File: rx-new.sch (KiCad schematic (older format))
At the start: 56 parts

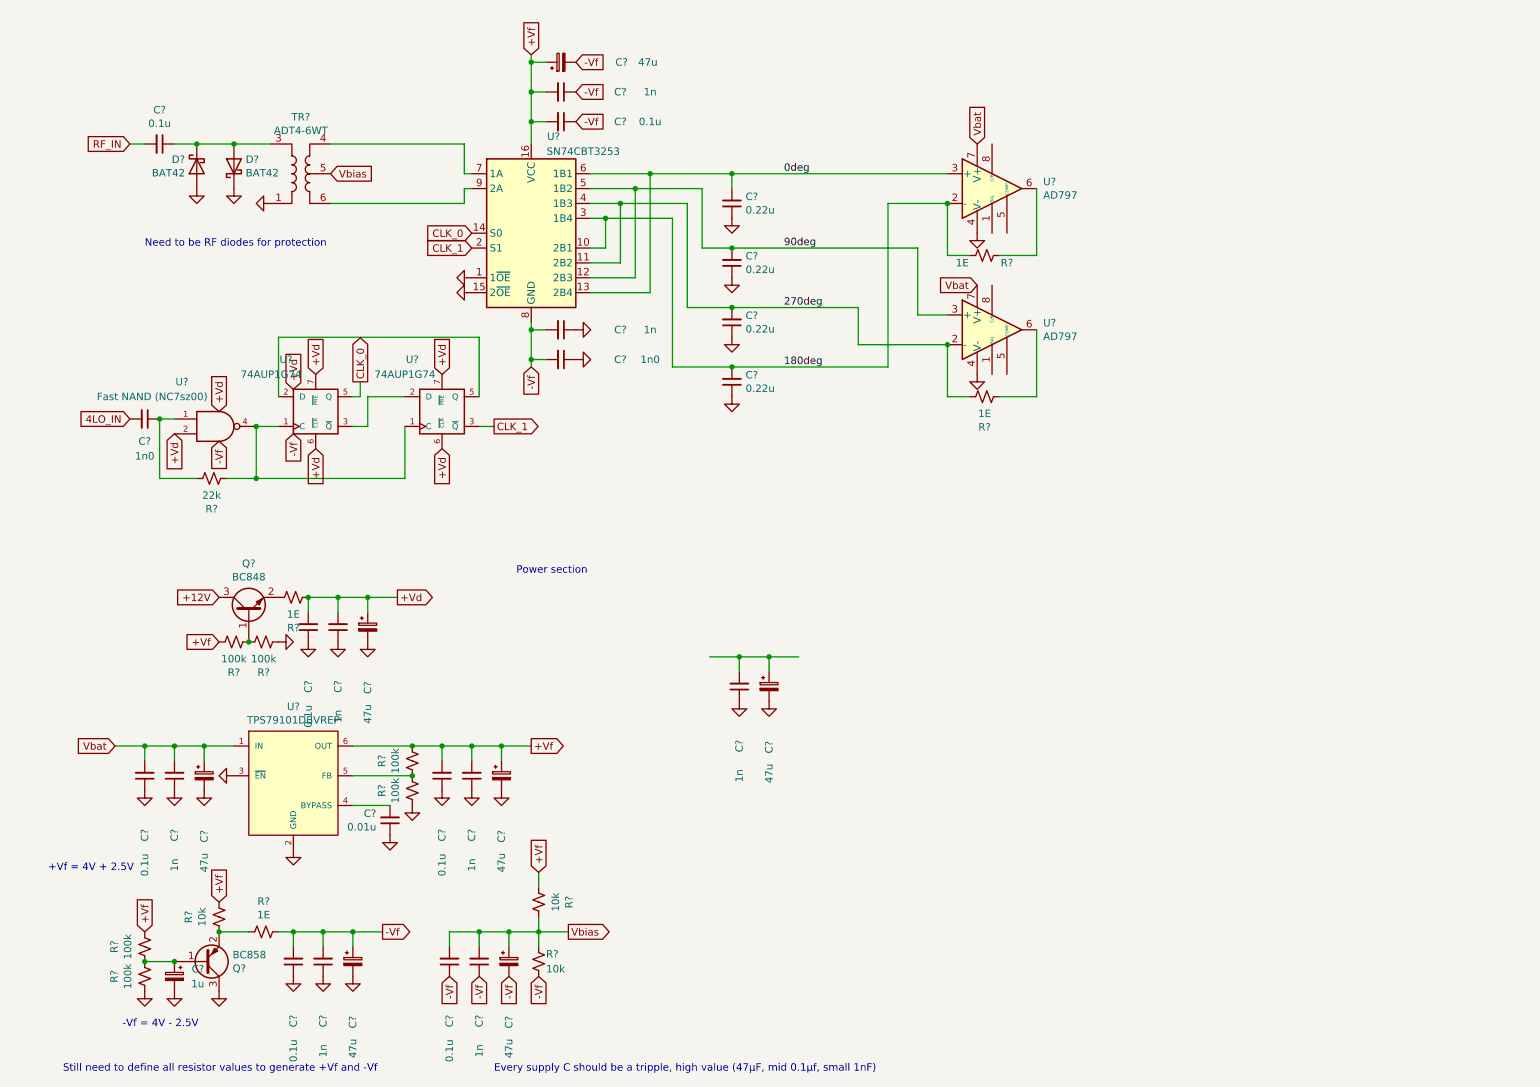
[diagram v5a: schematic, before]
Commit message: Added custom symbols for flipflops and nand buffer
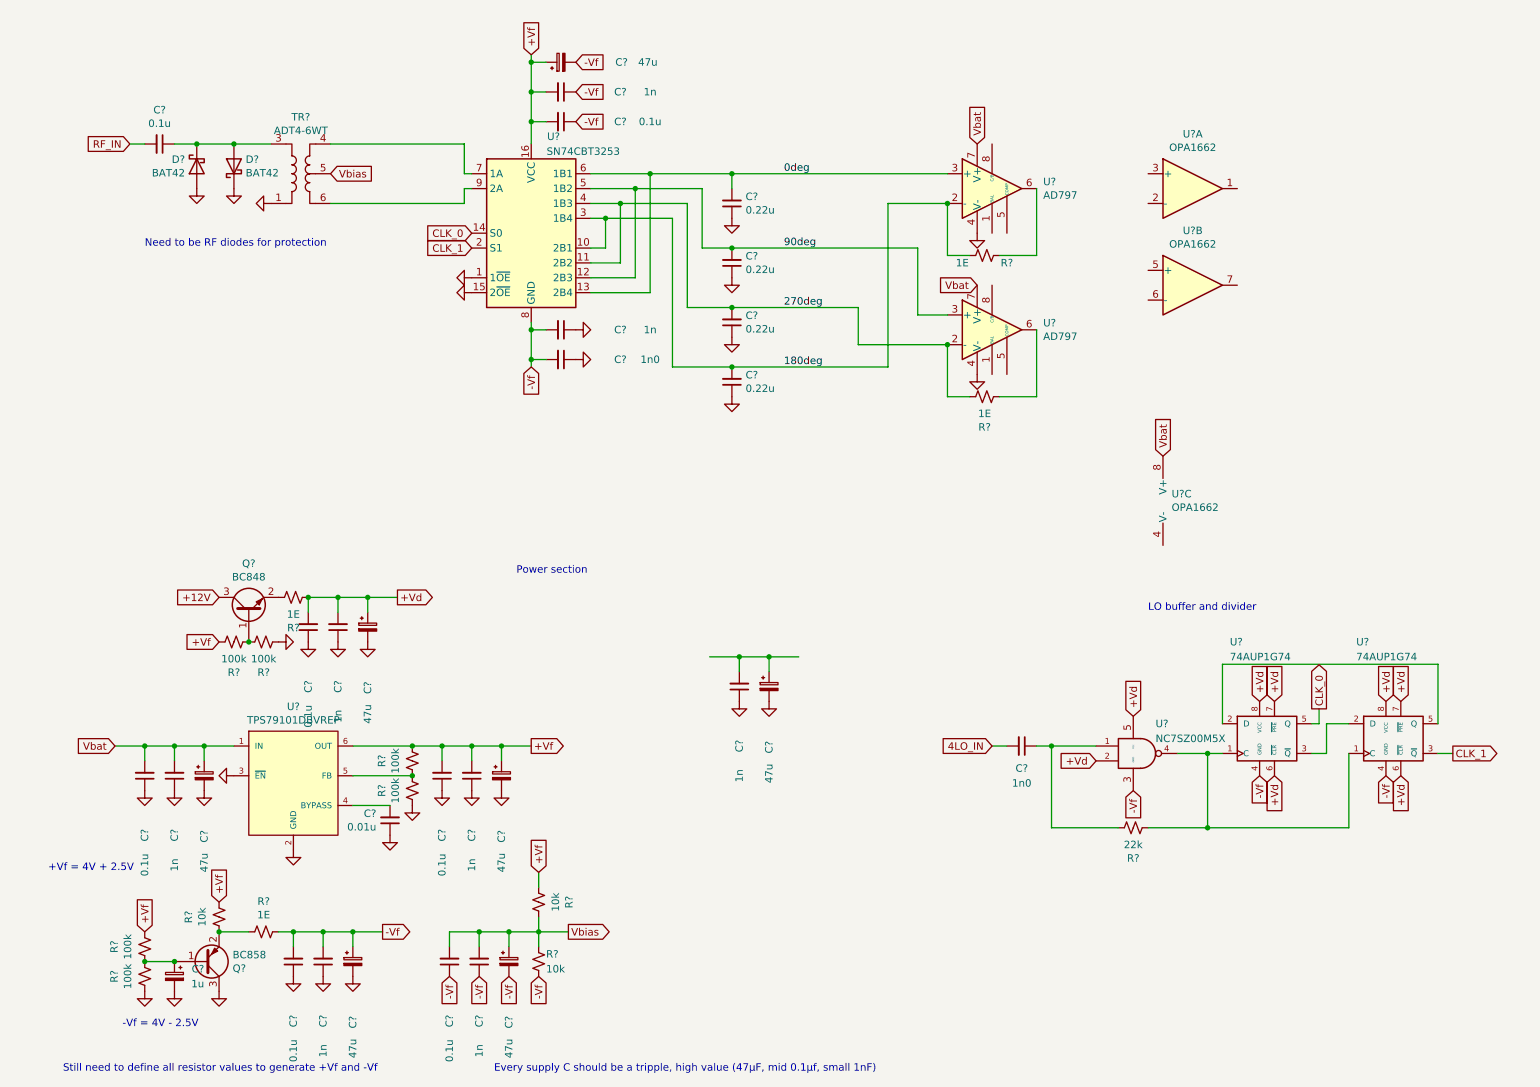
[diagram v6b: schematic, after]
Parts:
- removed U? (x2): 74AUP1G74, symbol 74xGxx:74AUP1G74
- removed U?: Fast NAND (NC7sz00), symbol 74xGxx:74LVC1G00
- added U? (x2): 74AUP1G74, Package_SO:VSSOP-8_2.4x2.1mm_P0.5mm, symbol custom_library:74AUP1G74
- added U? (x3): OPA1662, Package_SO:SOIC-8_3.9x4.9mm_P1.27mm, symbol Amplifier_Operational:OPA1602
- added U?: NC7SZ00M5X, Package_TO_SOT_SMD:SOT-23-5_HandSoldering, symbol custom_library:NC7SZ00M5X
- U?: footprint (none) -> Package_SO:SOP-16_4.4x10.4mm_P1.27mm
- U? (x2): footprint (none) -> Package_SO:SOIC-8_3.9x4.9mm_P1.27mm
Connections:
- net CLK_0: now also U?.5 (Q)
- net CLK_1: now also U?.3 (~Q)
- net GND: no longer C?.1, C?.1, C?.1, C?.1, C?.1, C?.2, C?.2, C?.2, C?.2, C?.2, C?.2, R?.1, R?.2, U?.8 (GND)
- net Vbat: now also U?.8 (V+)
- net at R?.2: now also U?.1 (C), U?.1 (C), U?.4
- net at C?.1, R?.1: now also U?.1
- net VCC renamed +Vd
- net +Vd: now also U?.2, U?.5 (Vcc), U?.6 (~CLR), U?.6 (~CLR), U?.7 (~PRE), U?.7 (~PRE), U?.8 (VCC), U?.8 (VCC)
- new net: U?.2 (D), U?.5 (Q)
- new net: U?.2 (D), U?.3 (~Q)
- new net -Vf: C?.1, C?.1, C?.1, C?.1, C?.1, C?.2, C?.2, C?.2, C?.2, C?.2, C?.2, R?.1, R?.2, U?.3 (GND), U?.4 (GND), U?.4 (GND), U?.8 (GND)
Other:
- note added: "LO buffer and divider"
- moved on the sheet: C?, R?
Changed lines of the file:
@@
 EESchema Schematic File Version 4
-LIBS:rx-new-cache
-EELAYER 29 0
+EELAYER 30 0
 EELAYER END
 $Descr A4 11693 8268
@@
 F 0 "U?" H 4100 2700 50  0000 C CNN
 F 1 "SN74CBT3253" H 4300 2600 50  0000 C CNN
-F 2 "" H 3950 2050 50  0001 C CNN
+F 2 "Package_SO:SOP-16_4.4x10.4mm_P1.27mm" H 3950 2050 50  0001 C CNN
 F 3 "http://www.ti.com/lit/gpn/sn74cbt3253" H 3950 2050 50  0001 C CNN
 	1    3950 2050
@@
 F 0 "U?" H 7394 1796 50  0000 L CNN
 F 1 "AD797" H 7394 1705 50  0000 L CNN
-F 2 "" H 7100 1800 50  0001 C CNN
+F 2 "Package_SO:SOIC-8_3.9x4.9mm_P1.27mm" H 7100 1800 50  0001 C CNN
 F 3 "https://www.analog.com/media/en/technical-documentation/data-sheets/AD797.pdf" H 7100 1900 50  0001 C CNN
 	1    7050 1750
@@
 F 3 "" H 5300 2750 50  0001 C CNN
 	1    5300 2750
-	1    0    0    -1
-$EndComp
-$Comp
-L power:GND #PWR?
-U 1 1 5F5B8768
-P 5300 3150
-F 0 "#PWR?" H 5300 2900 50  0001 C CNN
-F 1 "GND" H 5305 2977 50  0001 C CNN
-F 2 "" H 5300 3150 50  0001 C CNN
-F 3 "" H 5300 3150 50  0001 C CNN
-	1    5300 3150
 	1    0    0    -1
 $EndComp
@@
 Text Notes 3850 4350 0    50   ~ 0
 Power section
-$Comp
-L 74xGxx:74AUP1G74 U?
-U 1 1 5F5D87CB
-P 2500 3250
-F 0 "U?" H 2300 3600 50  0000 C CNN
-F 1 "74AUP1G74" H 2200 3500 50  0000 C CNN
-F 2 "" H 2500 3250 50  0001 C CNN
-F 3 "http://www.ti.com/lit/sg/scyt129e/scyt129e.pdf" H 2500 3250 50  0001 C CNN
-	1    2500 3250
-	1    0    0    -1
-$EndComp
-$Comp
-L 74xGxx:74AUP1G74 U?
-U 1 1 5F5D93F4
-P 3350 3250
-F 0 "U?" H 3150 3600 50  0000 C CNN
-F 1 "74AUP1G74" H 3100 3500 50  0000 C CNN
-F 2 "" H 3350 3250 50  0001 C CNN
-F 3 "http://www.ti.com/lit/sg/scyt129e/scyt129e.pdf" H 3350 3250 50  0001 C CNN
-	1    3350 3250
-	1    0    0    -1
-$EndComp
-Wire Wire Line
-	3600 3350 3700 3350
-Wire Wire Line
-	2750 3150 2800 3150
-Wire Wire Line
-	2800 3150 2800 3050
-Text GLabel 2800 3050 1    50   Output ~ 0
+Wire Wire Line
+	9250 5350 9250 5250
+Text GLabel 9250 5250 1    50   Output ~ 0
 CLK_0
-Text GLabel 3700 3350 2    50   Output ~ 0
-CLK_1
 Text GLabel 3950 2950 3    50   Input ~ 0
 -Vf
@@
 	3950 850  3950 900
 Wire Wire Line
-	2250 3150 2250 2750
-Wire Wire Line
-	2250 2750 3600 2750
-Wire Wire Line
-	3600 2750 3600 3150
-Wire Wire Line
-	2750 3350 2850 3350
-Wire Wire Line
-	2850 3350 2850 3150
-Wire Wire Line
-	2850 3150 3100 3150
+	8600 5350 8600 4950
+Wire Wire Line
+	9300 5550 9300 5350
+Wire Wire Line
+	9300 5350 9450 5350
 $Comp
 L Device:C_Small C?
@@
 Wire Wire Line
 	3500 1750 3550 1750
-Text GLabel 2350 3100 1    50   Input ~ 0
+Text GLabel 8850 5200 1    50   Input ~ 0
 +Vd
-Text GLabel 2350 3400 3    50   Input ~ 0
+Text GLabel 8850 5700 3    50   Input ~ 0
 -Vf
 $Comp
@@
 Wire Wire Line
 	2650 4500 2850 4500
-Text GLabel 2500 3000 1    50   Input ~ 0
+Text GLabel 8950 5200 1    50   Input ~ 0
 +Vd
-Text GLabel 3350 3000 1    50   Input ~ 0
-+Vd
-Text GLabel 2500 3500 3    50   Input ~ 0
-+Vd
-Text GLabel 3350 3500 3    50   Input ~ 0
+Text GLabel 8950 5700 3    50   Input ~ 0
 +Vd
 $Comp
@@
 F 0 "U?" H 7394 2746 50  0000 L CNN
 F 1 "AD797" H 7394 2655 50  0000 L CNN
-F 2 "" H 7100 2750 50  0001 C CNN
+F 2 "Package_SO:SOIC-8_3.9x4.9mm_P1.27mm" H 7100 2750 50  0001 C CNN
 F 3 "https://www.analog.com/media/en/technical-documentation/data-sheets/AD797.pdf" H 7100 2850 50  0001 C CNN
 	1    7050 2700
@@
 	0    -1   -1   0
 $EndComp
-Text GLabel 1850 3450 3    50   Input ~ 0
--Vf
-$Comp
-L 74xGxx:74LVC1G00 U?
-U 1 1 5F7DBBF0
-P 1850 3350
-F 0 "U?" H 1600 3650 50  0000 C CNN
-F 1 "Fast NAND (NC7sz00)" H 1400 3550 50  0000 C CNN
-F 2 "" H 1850 3350 50  0001 C CNN
-F 3 "http://www.ti.com/lit/sg/scyt129e/scyt129e.pdf" H 1850 3350 50  0001 C CNN
-	1    1850 3350
-	1    0    0    -1
-$EndComp
 $Comp
 L Device:R_Small_US R?
 U 1 1 5F7EB26C
-P 1800 3700
-F 0 "R?" V 1595 3700 50  0000 C CNN
-F 1 "22k" V 1686 3700 50  0000 C CNN
-F 2 "" H 1800 3700 50  0001 C CNN
-F 3 "~" H 1800 3700 50  0001 C CNN
-	1    1800 3700
+P 8000 6050
+F 0 "R?" V 7795 6050 50  0000 C CNN
+F 1 "22k" V 7886 6050 50  0000 C CNN
+F 2 "" H 8000 6050 50  0001 C CNN
+F 3 "~" H 8000 6050 50  0001 C CNN
+	1    8000 6050
 	0    -1   -1   0
 $EndComp
 Wire Wire Line
-	1900 3700 2100 3700
-Wire Wire Line
-	2100 3700 2100 3350
-Wire Wire Line
-	1700 3700 1450 3700
-Wire Wire Line
-	1450 3700 1450 3300
-Wire Wire Line
-	1450 3300 1550 3300
+	7900 6050 7450 6050
 $Comp
 L Device:C_Small C?
 U 1 1 5F7F5D47
-P 1350 3300
-F 0 "C?" V 1500 3300 50  0000 C CNN
-F 1 "1n0" V 1600 3300 50  0000 C CNN
-F 2 "" H 1350 3300 50  0001 C CNN
-F 3 "~" H 1350 3300 50  0001 C CNN
-	1    1350 3300
+P 7250 5500
+F 0 "C?" V 7400 5500 50  0000 C CNN
+F 1 "1n0" V 7500 5500 50  0000 C CNN
+F 2 "" H 7250 5500 50  0001 C CNN
+F 3 "~" H 7250 5500 50  0001 C CNN
+	1    7250 5500
 	0    1    1    0
 $EndComp
-Connection ~ 1450 3300
-Text GLabel 1250 3300 0    50   Input ~ 0
+Text GLabel 7050 5500 0    50   Input ~ 0
 4LO_IN
-Wire Wire Line
-	2100 3350 2250 3350
-Connection ~ 2100 3350
-Wire Wire Line
-	2100 3700 3100 3700
-Wire Wire Line
-	3100 3700 3100 3350
-Connection ~ 2100 3700
-Text GLabel 1550 3400 3    50   Input ~ 0
+$Comp
+L Amplifier_Operational:OPA1602 U?
+U 1 1 5F62CDCA
+P 8400 1750
+F 0 "U?" H 8400 2117 50  0000 C CNN
+F 1 "OPA1662" H 8400 2026 50  0000 C CNN
+F 2 "Package_SO:SOIC-8_3.9x4.9mm_P1.27mm" H 8400 1750 50  0001 C CNN
+F 3 "http://www.ti.com/lit/ds/symlink/opa1662.pdf" H 8400 1750 50  0001 C CNN
+	1    8400 1750
+	1    0    0    -1
+$EndComp
+$Comp
+L Amplifier_Operational:OPA1602 U?
+U 2 1 5F62F9A9
+P 8400 2400
+F 0 "U?" H 8400 2767 50  0000 C CNN
+F 1 "OPA1662" H 8400 2676 50  0000 C CNN
+F 2 "Package_SO:SOIC-8_3.9x4.9mm_P1.27mm" H 8400 2400 50  0001 C CNN
+F 3 "http://www.ti.com/lit/ds/symlink/opa1662.pdf" H 8400 2400 50  0001 C CNN
+	2    8400 2400
+	1    0    0    -1
+$EndComp
+$Comp
+L Amplifier_Operational:OPA1602 U?
+U 3 1 5F633584
+P 8300 3850
+F 0 "U?" H 8258 3896 50  0000 L CNN
+F 1 "OPA1662" H 8258 3805 50  0000 L CNN
+F 2 "Package_SO:SOIC-8_3.9x4.9mm_P1.27mm" H 8300 3850 50  0001 C CNN
+F 3 "http://www.ti.com/lit/ds/symlink/opa1662.pdf" H 8300 3850 50  0001 C CNN
+	3    8300 3850
+	1    0    0    -1
+$EndComp
+Text GLabel 8200 3550 1    50   Input ~ 0
+Vbat
+$Comp
+L custom_library:74AUP1G74 U?
+U 1 1 5F5FE082
+P 8950 5450
+F 0 "U?" H 8650 6100 50  0000 L CNN
+F 1 "74AUP1G74" H 8650 6000 50  0000 L CNN
+F 2 "Package_SO:VSSOP-8_2.4x2.1mm_P0.5mm" H 8950 5450 50  0001 C CNN
+F 3 "https://assets.nexperia.com/documents/data-sheet/74AUP1G74.pdf" H 8950 5450 50  0001 C CNN
+	1    8950 5450
+	1    0    0    -1
+$EndComp
+Wire Wire Line
+	8600 5550 8500 5550
+Wire Wire Line
+	9200 5350 9250 5350
+Wire Wire Line
+	9200 5550 9300 5550
+Wire Wire Line
+	8100 6050 8500 6050
+Wire Wire Line
+	8500 5550 8500 6050
+Connection ~ 8500 5550
+Wire Wire Line
+	8500 5550 8300 5550
+Connection ~ 8500 6050
+Wire Wire Line
+	8500 6050 9450 6050
+Wire Wire Line
+	9450 5550 9450 6050
+Wire Wire Line
+	7450 5500 7450 6050
+Text GLabel 10150 5550 2    50   Output ~ 0
+CLK_1
+Wire Wire Line
+	10050 5550 10150 5550
+Text GLabel 9800 5200 1    50   Input ~ 0
 +Vd
-Text GLabel 1850 3250 1    50   Input ~ 0
+Text GLabel 9700 5200 1    50   Input ~ 0
 +Vd
+Text GLabel 9700 5700 3    50   Input ~ 0
+-Vf
+Text GLabel 9800 5700 3    50   Input ~ 0
++Vd
+$Comp
+L custom_library:74AUP1G74 U?
+U 1 1 5F655934
+P 9800 5450
+F 0 "U?" H 9500 6100 50  0000 L CNN
+F 1 "74AUP1G74" H 9500 6000 50  0000 L CNN
+F 2 "Package_SO:VSSOP-8_2.4x2.1mm_P0.5mm" H 9800 5450 50  0001 C CNN
+F 3 "https://assets.nexperia.com/documents/data-sheet/74AUP1G74.pdf" H 9800 5450 50  0001 C CNN
+	1    9800 5450
+	1    0    0    -1
+$EndComp
+$Comp
+L power:GND #PWR?
+U 1 1 5F5B8768
+P 5300 3150
+F 0 "#PWR?" H 5300 2900 50  0001 C CNN
+F 1 "GND" H 5305 2977 50  0001 C CNN
+F 2 "" H 5300 3150 50  0001 C CNN
+F 3 "" H 5300 3150 50  0001 C CNN
+	1    5300 3150
+	1    0    0    -1
+$EndComp
+Wire Wire Line
+	10050 4950 10050 5350
+Wire Wire Line
+	8600 4950 10050 4950
+$Comp
+L custom_library:NC7SZ00M5X U?
+U 1 1 5F69D911
+P 8050 5550
+F 0 "U?" H 8150 5750 50  0000 L CNN
+F 1 "NC7SZ00M5X" H 8150 5650 50  0000 L CNN
+F 2 "Package_TO_SOT_SMD:SOT-23-5_HandSoldering" H 8050 5550 50  0001 C CNN
+F 3 "https://ro.mouser.com/datasheet/2/308/NC7SZ00-D-1812355.pdf" H 8050 5550 50  0001 C CNN
+	1    8050 5550
+	1    0    0    -1
+$EndComp
+Text GLabel 8000 5300 1    50   Input ~ 0
++Vd
+Text GLabel 8000 5800 3    50   Input ~ 0
+-Vf
+Text GLabel 7750 5600 0    50   Input ~ 0
++Vd
+Wire Wire Line
+	7450 5500 7750 5500
+Wire Wire Line
+	7050 5500 7150 5500
+Wire Wire Line
+	7350 5500 7450 5500
+Connection ~ 7450 5500
+Text Notes 8100 4600 0    50   ~ 0
+LO buffer and divider
 $EndSCHEMATC

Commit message: level_shifter
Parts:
- removed C?: 1u, symbol Device:CP_Small
- removed R?: 1E, symbol Device:R_Small_US
- added C? (x2): 0.1u, symbol Device:C_Small
- added R? (x3): 1E, symbol Device:R_Small_US
- added R? (x6): 2.7k, symbol Device:R_Small_US
- added R? (x2): 390E, symbol Device:R_Small_US
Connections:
- net +12V is gone; now on net Vbat: Q?.3 (C)
- net +Vd: now also R?.1
- net +Vf: now also U?.8 (V+), R?.1, R?.1
- net -Vf: now also U?.1 (1~OE), U?.15 (2~OE)
- net GND: now also U?.4 (V-); no longer U?.1 (1~OE), U?.15 (2~OE)
- net Vbat: no longer U?.8 (V+)
- net Vbias: now also U?.3 (+), U?.5 (+)
- net at R?.2, U?.6: now also R?.1 (x2)
- net at Q?.1 (B), R?.1, R?.2: now also C?.1
- net at Q?.2 (E), R?.2, R?.2: now also C?.2
- net at U?.1: now also R?.1, R?.2
- net at U?.2 (-): now also R?.1, R?.2, R?.2
- net at U?.6 (-): now also R?.1, R?.2, R?.2
- net at U?.7: now also R?.1, R?.2
- net at Q?.1 (B), R?.1, R?.2: now also C?.2
- net at Q?.2 (E): now also C?.1, R?.2
- new net: R?.1, R?.2 (x2)
- new net I: R?.2
- new net Q: R?.2
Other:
- note added: "+Vf = 6.5V"
- note added: "-Vf = 1.5V"
- note added: "1.65V DC"
- note added: "4V DC"
- note added: "Need to be BAT64-04"
- note removed: "+Vf = 4V + 2.5V"
- note removed: "-Vf = 4V - 2.5V"
- note removed: "Need to be RF diodes for protection"
- moved on the sheet: Q?, R?, U?A, U?B, U?C
